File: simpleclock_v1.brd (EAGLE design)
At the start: 80 x 80 mm, 88 parts, among them IC1 TINY24/44/84-SSU

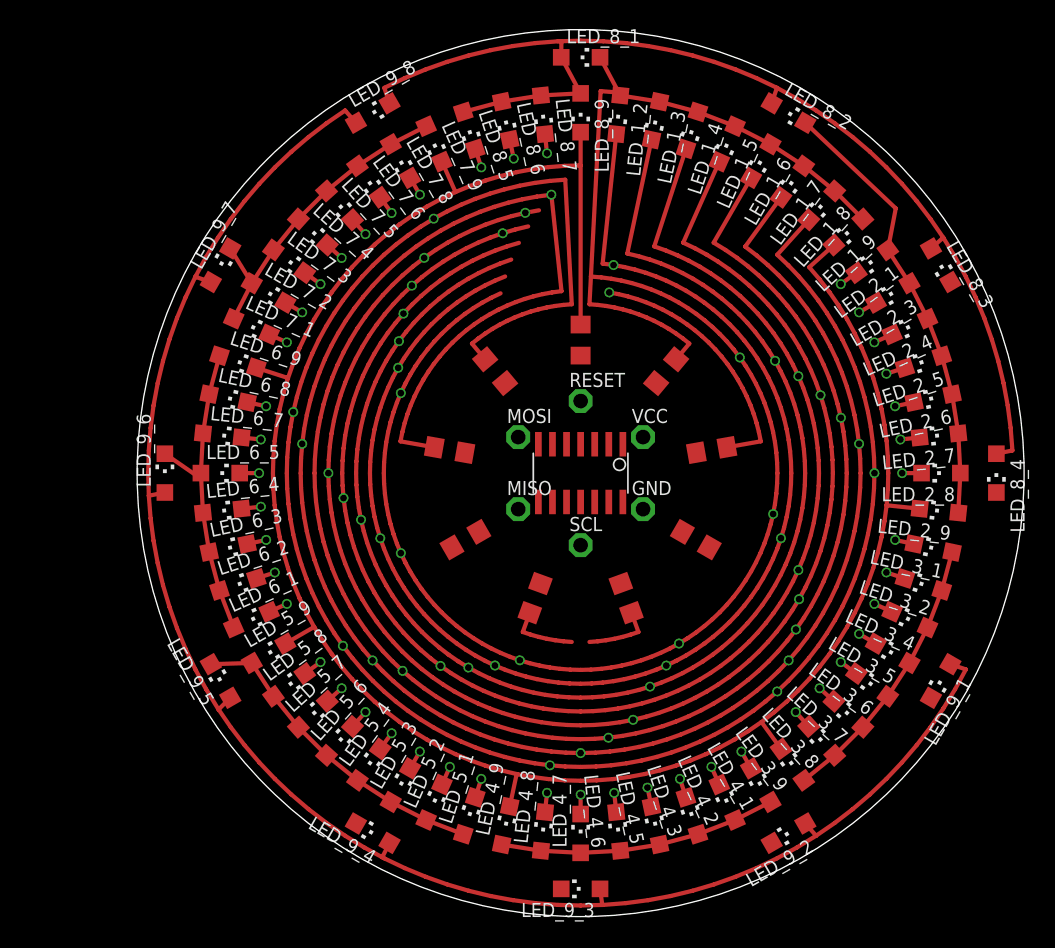
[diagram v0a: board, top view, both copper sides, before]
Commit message: lots more traces routed
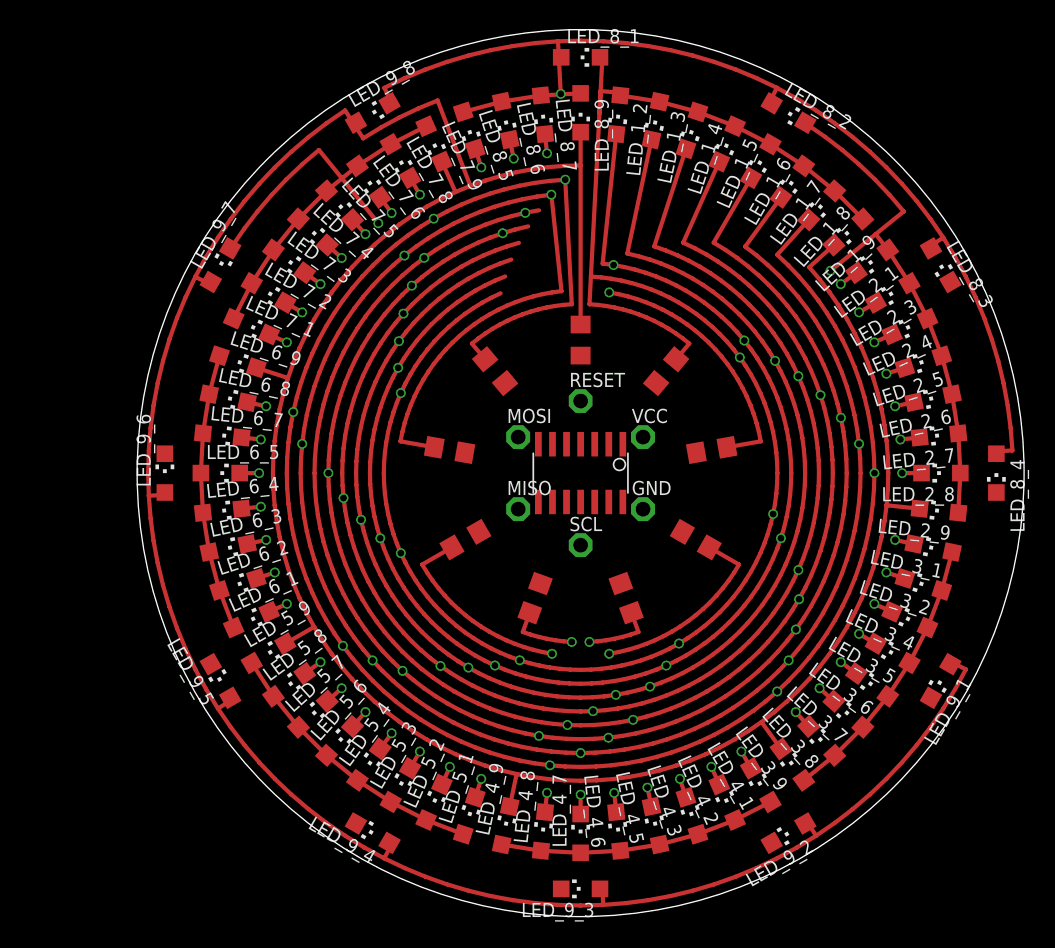
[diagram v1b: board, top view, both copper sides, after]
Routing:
- net N_3: track 161.0 -> 178.6 mm, vias 10 -> 12
- net N_9: track 344.1 -> 361.6 mm
- net N_7: track 218.0 -> 234.6 mm, vias 12 -> 14
- net N_6: track 180.8 -> 194.5 mm, vias 12 -> 14
- net N_2: track 194.5 -> 201.5 mm, vias 12 -> 14
- net N_5: track 182.2 -> 178.5 mm, vias 12 -> 14
- net N_1: track 175.3 -> 176.4 mm
- net N_8: track 282.7 -> 282.4 mm, vias 12 -> 14
- net N_4: vias 10 -> 12

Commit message: wow, it's been that long since i committed?
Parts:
- added RDOWN, RUP: (no value), SparkFun:1206
- moved RESET 1.50 mm to (40.0, 48.0)
- moved SCL 1.50 mm to (40.0, 32.0)
- moved GND 1.50 mm to (46.9, 36.0)
- moved MISO 1.50 mm to (33.1, 36.0)
- moved MOSI 1.50 mm to (33.1, 44.0)
- moved VCC 1.50 mm to (46.9, 44.0)
- turned RN1 to 320 degrees
- turned RN2 to 280 degrees
- turned RN3 to 60 degrees
- turned RN4 to 20 degrees
- turned RN5 to 160 degrees
- turned RN6 to 120 degrees
- turned RN7 to 260 degrees
- turned RN8 to 220 degrees
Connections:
- net N$1 renamed PB2
- net N$2 renamed PA7
- net N$3 renamed PA6
- net N$4 renamed PA5
- net N$5 renamed PA4
- net N$6 renamed PA3
- net N$7 renamed PA2
- net N$8 renamed PA1
- net N$9 renamed PA0
- removed net N$10: IC1.3
- removed net N$11: IC1.2
- removed net N$20: IC1.4, RESET.TP
- new net PB0: IC1.2, RUP.2
- new net PB1: IC1.3, RDOWN.2
- new net PB3: IC1.4, RDOWN.1, RESET.TP, RUP.1
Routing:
- net N_3: track 178.6 -> 302.6 mm, vias 12 -> 14
- net N_4: track 172.1 -> 272.8 mm, vias 12 -> 16
- net N_1: track 176.4 -> 273.9 mm, vias 12 -> 14
- net N_2: track 201.5 -> 285.8 mm, vias 14 -> 16
- net N_6: track 194.5 -> 262.6 mm, vias 14 -> 16
- net N_5: track 178.5 -> 244.7 mm, vias 14 -> 16
- net PA0: track 0.00 -> 30.4 mm
- net N_7: track 234.6 -> 264.4 mm
- net N_8: track 282.4 -> 309.5 mm
- net PA1: track 0.00 -> 13.4 mm
- net PA2: track 0.00 -> 12.2 mm
- net PB3: track 0.00 -> 11.7 mm
- net PA4: track 0.00 -> 11.3 mm
- net PA3: track 0.00 -> 10.8 mm
- net PA7: track 0.00 -> 9.19 mm
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- added copper zone on layer 16, net PB0
- added copper zone on layer 16, net PB1

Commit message: new board outline
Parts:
- added IC2: MEGA48/88/168-AU, avr-7:TQFP32-08
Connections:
- new net AGND: IC2.21
- net GND: now also IC2.3, IC2.5
- net VCC: now also IC2.4, IC2.6
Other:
- outline, holes or cut-outs redrawn
